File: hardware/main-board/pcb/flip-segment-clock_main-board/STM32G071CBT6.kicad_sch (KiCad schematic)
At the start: 1 part, among them IC1 STM32G071CBT6

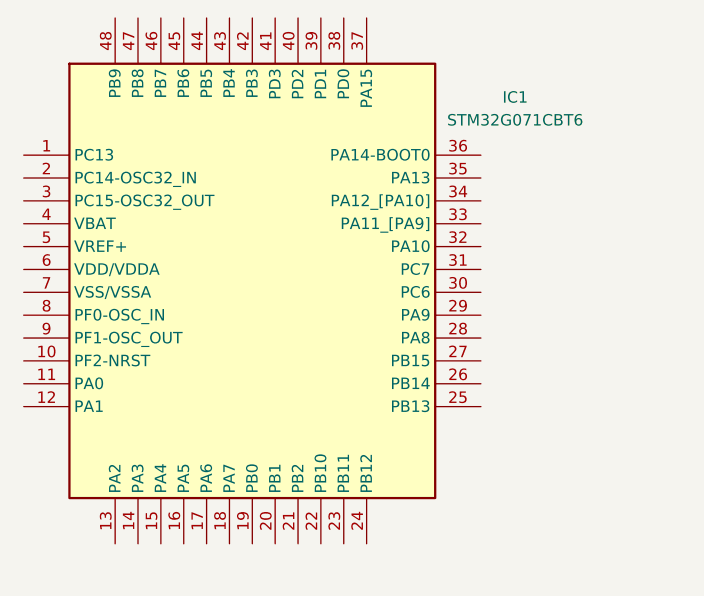
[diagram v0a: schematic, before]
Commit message: Refining design of the segment drivers
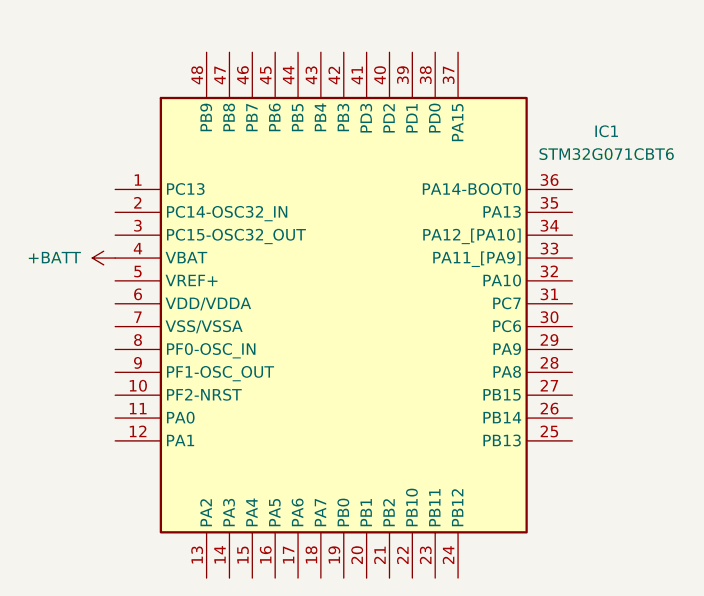
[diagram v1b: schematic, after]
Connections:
- net +BATT: now reaches IC1.4 (VBAT)
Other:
- moved on the sheet: IC1
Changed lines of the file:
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@@
 	(paper "A4")
 	(symbol
+		(lib_id "power:+BATT")
+		(at 64.77 74.93 90)
+		(unit 1)
+		(exclude_from_sim no)
+		(in_bom yes)
+		(on_board yes)
+		(dnp no)
+		(fields_autoplaced yes)
+		(property "Reference" "#PWR05"
+			(at 68.58 74.93 0)
+			(effects
+				(font
+					(size 1.27 1.27)
+				)
+				(hide yes)
+			)
+		)
+		(property "Value" "+BATT"
+			(at 60.96 74.9299 90)
+			(effects
+				(font
+					(size 1.27 1.27)
+				)
+				(justify left)
+			)
+		)
+		(property "Footprint" ""
+			(at 64.77 74.93 0)
+			(effects
+				(font
+					(size 1.27 1.27)
+				)
+				(hide yes)
+			)
+		)
+		(property "Datasheet" ""
+			(at 64.77 74.93 0)
+			(effects
+				(font
+					(size 1.27 1.27)
+				)
+				(hide yes)
+			)
+		)
+		(property "Description" "Power symbol creates a global label with name \"+BATT\""
+			(at 64.77 74.93 0)
+			(effects
+				(font
+					(size 1.27 1.27)
+				)
+				(hide yes)
+			)
+		)
+		(pin "1"
+		)
+		(instances
+			(project ""
+				(path "/831ae1ef-1bd9-4f70-83f4-283bc54c43f2/7c23a0e0-12b9-4301-b469-91a3098c81d4"
+					(reference "#PWR05")
+					(unit 1)
+				)
+			)
+		)
+	)
+	(symbol
 		(lib_id "STM32G071CBT6:STM32G071CBT6")
-		(at 54.61 63.5 0)
+		(at 64.77 67.31 0)
 		(unit 1)
 		(exclude_from_sim no)
@@
 		(fields_autoplaced yes)
 		(property "Reference" "IC1"
-			(at 109.22 57.0798 0)
+			(at 119.38 60.8898 0)
 			(effects
 				(font
@@
 		)
 		(property "Value" "STM32G071CBT6"
-			(at 109.22 59.6198 0)
+			(at 119.38 63.4298 0)
 			(effects
 				(font
@@
 		)
 		(property "Footprint" "STM32G071CBT6:QFP50P900X900X160-48N"
-			(at 101.6 150.8 0)
+			(at 111.76 154.61 0)
 			(effects
 				(font
@@
 		)
 		(property "Datasheet" "https://www.st.com/resource/en/datasheet/stm32g071c8.pdf"
-			(at 101.6 250.8 0)
+			(at 111.76 254.61 0)
 			(effects
 				(font
@@
 		)
 		(property "Description" "Arm Cortex-M0+ 32-bit MCU, up to 128 KB Flash, 36 KB RAM, 4x USART, timers, ADC, DAC, comm. I/Fs, 1.7-3.6V"
-			(at 54.61 63.5 0)
+			(at 64.77 67.31 0)
 			(effects
 				(font
@@
 		)
 		(property "Height" "1.6"
-			(at 101.6 450.8 0)
+			(at 111.76 454.61 0)
 			(effects
 				(font
@@
 		)
 		(property "Mouser Part Number" "511-STM32G071CBT6"
-			(at 101.6 550.8 0)
+			(at 111.76 554.61 0)
 			(effects
 				(font
@@
 		)
 		(property "Mouser Price/Stock" "https://www.mouser.co.uk/ProductDetail/STMicroelectronics/STM32G071CBT6?qs=PqoDHHvF648kq6bRqLhyjQ%3D%3D"
-			(at 101.6 650.8 0)
+			(at 111.76 654.61 0)
 			(effects
 				(font
@@
 		)
 		(property "Manufacturer_Name" "STMicroelectronics"
-			(at 101.6 750.8 0)
+			(at 111.76 754.61 0)
 			(effects
 				(font
@@
 		)
 		(property "Manufacturer_Part_Number" "STM32G071CBT6"
-			(at 101.6 850.8 0)
+			(at 111.76 854.61 0)
 			(effects
 				(font
@@
 		)
 		(property "LCSC Part Number" "C432212"
-			(at 54.61 63.5 0)
+			(at 64.77 67.31 0)
 			(effects
 				(font
@@
 				)
 			)
+			(project "STM32G071CBT6"
+				(path "/99f7b8c9-94b2-4f71-8e96-e9b3d6ac7e41"
+					(reference "IC?")
+					(unit 1)
+				)
+			)
 		)
 	)
+	(sheet_instances
+		(path "/"
+			(page "1")
+		)
+	)
+	(embedded_fonts no)
 )
